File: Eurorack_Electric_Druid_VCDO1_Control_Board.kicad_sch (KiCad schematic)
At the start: 0 parts

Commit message: Multiboard work update
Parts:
- added C20, C21, C22, C23: 0.1uF, DIYSynthMNL:C_Rect_L7.0mm_W2.0mm_P5.00mm_BigPads, symbol Device:C
- added H1, H2: MountingHole_Pad, DIYSynthMNL:MountingHole_M3_Standoff_Pad, symbol Mechanical:MountingHole_Pad
- added J10: Glide_time_CV_in, DIYSynthMNL:AudioJack_3.5mm_long_pads, symbol DIYSynthMNL:PJ3001F
- added J11: Bitcrush_CV_in, DIYSynthMNL:AudioJack_3.5mm_long_pads, symbol DIYSynthMNL:PJ3001F
- added J3: Main_osc_out, DIYSynthMNL:AudioJack_3.5mm_long_pads, symbol DIYSynthMNL:PJ3001F
- added J4: Sub_osc_out, DIYSynthMNL:AudioJack_3.5mm_long_pads, symbol DIYSynthMNL:PJ3001F
- added J5: Glide_on_off_CV_in, DIYSynthMNL:AudioJack_3.5mm_long_pads, symbol DIYSynthMNL:PJ3001F
- added J6: Note_CV_in, DIYSynthMNL:AudioJack_3.5mm_long_pads, symbol DIYSynthMNL:PJ3001F
- added J7: FM_CV_in, DIYSynthMNL:AudioJack_3.5mm_long_pads, symbol DIYSynthMNL:PJ3001F
- added J8: WaveSel_CV_in, DIYSynthMNL:AudioJack_3.5mm_long_pads, symbol DIYSynthMNL:PJ3001F
- added J9: SubSel_CV_in, DIYSynthMNL:AudioJack_3.5mm_long_pads, symbol DIYSynthMNL:PJ3001F
- added R23: 10K, DIYSynthMNL:R_quarter_watt_L6.3mm_D2.5mm_P7.62mm, symbol Device:R
- added R40, R41, R42, R43: 1K, DIYSynthMNL:R_quarter_watt_L6.3mm_D2.5mm_P7.62mm, symbol Device:R
- added RV10: 10K_SubWaveSel, DIYSynthMNL:Potentiometer_RV09_BigPads, symbol Device:R_Potentiometer
- added RV13: 100K_GlideTime_CV_Amount, DIYSynthMNL:Potentiometer_RV09_BigPads, symbol Device:R_Potentiometer
- added RV14: 100K_GlideTime, DIYSynthMNL:Potentiometer_RV09_BigPads, symbol Device:R_Potentiometer
- added RV15: 100K_Bitcrush, DIYSynthMNL:Potentiometer_RV09_BigPads, symbol Device:R_Potentiometer
- added RV16: 100K_Bitcrush_CV_Amount, DIYSynthMNL:Potentiometer_RV09_BigPads, symbol Device:R_Potentiometer
- added RV3: 100K_FM_CV_Amount, DIYSynthMNL:Potentiometer_RV09_BigPads, symbol Device:R_Potentiometer
- added RV5: 100K_WaveSel_CV_Amount, DIYSynthMNL:Potentiometer_RV09_BigPads, symbol Device:R_Potentiometer
- added RV6: 100K_SubSel_CV_Amount, DIYSynthMNL:Potentiometer_RV09_BigPads, symbol Device:R_Potentiometer
- added RV7: 10K_Freq_Course, DIYSynthMNL:Potentiometer_RV09_BigPads, symbol Device:R_Potentiometer
- added RV8: 10K_Freq_Fine, DIYSynthMNL:Potentiometer_RV09_BigPads, symbol Device:R_Potentiometer
- added RV9: 10K_MainWaveSel, DIYSynthMNL:Potentiometer_RV09_BigPads, symbol Device:R_Potentiometer
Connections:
- new net: R42.2, RV9.2
- new net: J10.T, RV13.3
- new net: J7.T, RV3.3
- new net: J11.TN, RV15.2
- new net: J11.T, RV16.3
- new net: R43.2, RV10.2
- new net: J5.TN, R23.2
- new net: J9.T, RV6.3
- new net: J8.T, RV5.3
- new net: J10.TN, RV14.2
- new net: R41.2, RV8.2
- new net: R40.2, RV7.2
- new net Bitcrush_CV: RV16.2
- new net CB_+5V: R23.1, RV10.3, RV14.3, RV15.3, RV7.3, RV8.3, RV9.3
- new net CB_-5V: RV14.1, RV15.1
- new net CB_GND: C20.2, C21.2, C22.2, C23.2, H1.1, H2.1, J10.S, J11.S, J3.S, J4.S, J5.S, J6.S, RV10.1, RV13.1, RV16.1, RV3.1, RV5.1, RV6.1, RV7.1, RV8.1, RV9.1
- new net FM_CV: RV3.2
- new net Freq_Course_Ctrl: C20.1, R40.1
- new net Freq_Fine_Ctrl: C21.1, R41.1
- new net GND: J7.S, J8.S, J9.S
- new net Glide_OnOff_CV: J5.T
- new net Glide_Time_CV: RV13.2
- new net MainOsc_Out: J3.T
- new net MainWaveSel_CV: RV5.2
- new net MainWaveSel_Ctrl: C22.1, R42.1
- new net Note_CV: J6.T
- new net SubOsc_Out: J4.T
- new net SubWaveSel_CV: RV6.2
- new net SubWaveSel_Ctrl: C23.1, R43.1
- no-connect marks 0 -> 6
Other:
- note added: "+/-5V"
- note added: "0V-5V"
- note added: "0V/5V"
- note added: "10vpp in"
- note added: "Bitcrush CV"
- note added: "Controls/Pots"
- note added: "FM CV"
- note added: "Glide CV"
- note added: "Glide on/off CV"
- note added: "Main Wave Select CV"
- note added: "Note CV"
- note added: "Pots inverted on purpose!"
- note added: "Sub Wave Select CV"

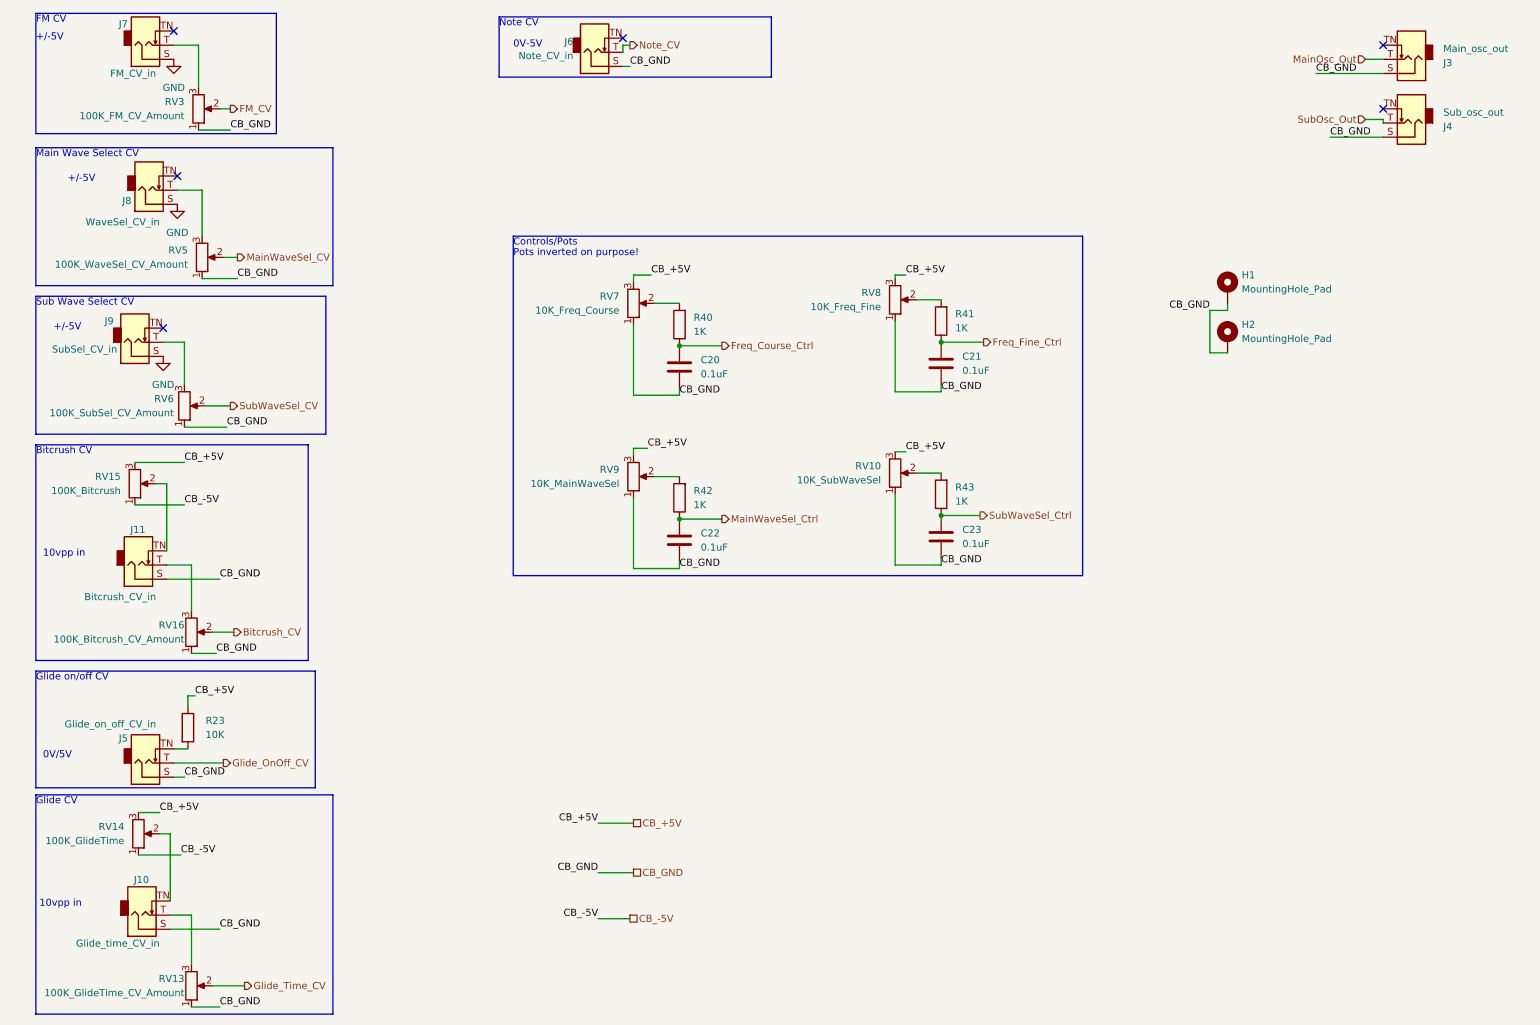
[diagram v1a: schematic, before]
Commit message: updated schematic to rev 0.1.1
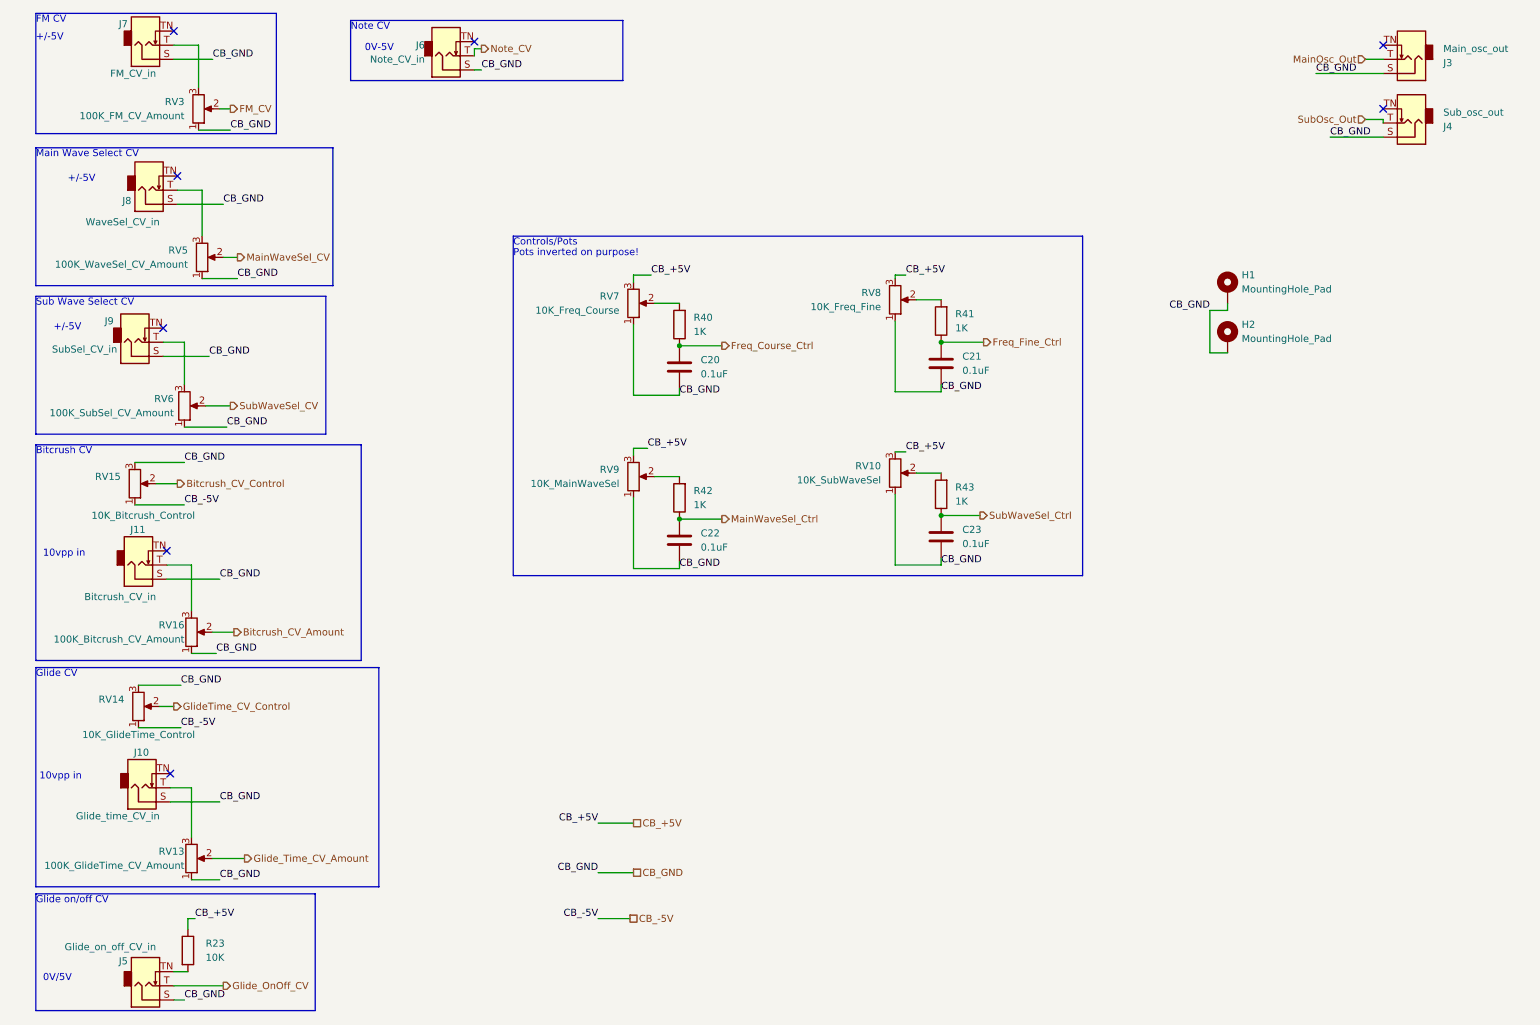
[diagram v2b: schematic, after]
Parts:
- RV14: value 100K_GlideTime -> 10K_GlideTime_Control
- RV15: value 100K_Bitcrush -> 10K_Bitcrush_Control
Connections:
- net GND is gone; now on net CB_GND: J7.S, J8.S, J9.S
- net CB_+5V: no longer RV14.3, RV15.3
- net CB_GND: now also RV14.3, RV15.3
- net at J11.TN: no longer RV15.2
- net at J10.TN: no longer RV14.2
- net Bitcrush_CV renamed Bitcrush_CV_Amount
- net Glide_Time_CV renamed Glide_Time_CV_Amount
- new net Bitcrush_CV_Control: RV15.2
- new net GlideTime_CV_Control: RV14.2
- no-connect marks 6 -> 8
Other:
- moved on the sheet: J10, J5, J6, R23, RV13, RV14

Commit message: updated to schematic revision 1.2
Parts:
- renumbered H1 to H3, H2 to H4
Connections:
- net CB_+5V: now also RV10.1, RV7.1, RV8.1, RV9.1; no longer RV10.3, RV7.3, RV8.3, RV9.3
- net CB_GND: now also RV10.3, RV7.3, RV8.3, RV9.3; no longer RV10.1, RV7.1, RV8.1, RV9.1
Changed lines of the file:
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@@
     (title "Eurorack Electric Druid VCDO1 - Control Board")
     (date "2023-12-30")
-    (rev "0.1.1")
+    (rev "0.1.2")
     (company "DIYSynthMNL")
     (comment 1 "Shared under a CC BY-NC-SA 4.0 license. Some rights reserved.")
@@
   (symbol (lib_id "Mechanical:MountingHole_Pad") (at 227.33 74.295 0) (unit 1)
     (in_bom yes) (on_board yes) (dnp no) (fields_autoplaced)
-    (property "Reference" "H2" (at 229.87 71.755 0)
+    (property "Reference" "H4" (at 229.87 71.755 0)
       (effects (font (size 1.27 1.27)) (justify left))
     )
@@
       (project "Electric Druid VCDO1"
         (path "/1a79e409-2950-446e-9b6e-16f6bf0a888d/c68a14c9-390d-4940-8b6e-7a8e2ca87292"
-          (reference "H2") (unit 1)
+          (reference "H4") (unit 1)
         )
       )
@@
         )
         (path "/1a79e409-2950-446e-9b6e-16f6bf0a888d/c68a14c9-390d-4940-8b6e-7a8e2ca87292"
-          (reference "R42") (unit 1)
+          (reference "R50") (unit 1)
         )
       )
@@
         )
         (path "/1a79e409-2950-446e-9b6e-16f6bf0a888d/c68a14c9-390d-4940-8b6e-7a8e2ca87292"
-          (reference "J7") (unit 1)
+          (reference "J5") (unit 1)
         )
       )
@@
     )
   )
-  (symbol (lib_id "Device:R_Potentiometer") (at 167.64 98.425 0) (mirror x) (unit 1)
-    (in_bom yes) (on_board yes) (dnp no)
-    (property "Reference" "RV10" (at 165.1 97.155 0)
-      (effects (font (size 1.27 1.27)) (justify right))
-    )
-    (property "Value" "10K_SubWaveSel" (at 165.1 99.695 0)
+  (symbol (lib_id "Device:R_Potentiometer") (at 167.64 98.425 0) (unit 1)
+    (in_bom yes) (on_board yes) (dnp no)
+    (property "Reference" "RV10" (at 165.1 99.695 0)
+      (effects (font (size 1.27 1.27)) (justify right))
+    )
+    (property "Value" "10K_SubWaveSel" (at 165.1 97.155 0)
       (effects (font (size 1.27 1.27)) (justify right))
     )
@@
         )
         (path "/1a79e409-2950-446e-9b6e-16f6bf0a888d/c68a14c9-390d-4940-8b6e-7a8e2ca87292"
-          (reference "RV10") (unit 1)
+          (reference "RV9") (unit 1)
         )
       )
@@
         )
         (path "/1a79e409-2950-446e-9b6e-16f6bf0a888d/c68a14c9-390d-4940-8b6e-7a8e2ca87292"
-          (reference "C22") (unit 1)
+          (reference "C24") (unit 1)
         )
       )
@@
         )
         (path "/1a79e409-2950-446e-9b6e-16f6bf0a888d/c68a14c9-390d-4940-8b6e-7a8e2ca87292"
-          (reference "J10") (unit 1)
+          (reference "J11") (unit 1)
         )
       )
@@
         )
         (path "/1a79e409-2950-446e-9b6e-16f6bf0a888d/c68a14c9-390d-4940-8b6e-7a8e2ca87292"
-          (reference "R23") (unit 1)
+          (reference "R51") (unit 1)
         )
       )
@@
         )
         (path "/1a79e409-2950-446e-9b6e-16f6bf0a888d/c68a14c9-390d-4940-8b6e-7a8e2ca87292"
-          (reference "J9") (unit 1)
+          (reference "J10") (unit 1)
         )
       )
@@
         )
         (path "/1a79e409-2950-446e-9b6e-16f6bf0a888d/c68a14c9-390d-4940-8b6e-7a8e2ca87292"
-          (reference "J3") (unit 1)
+          (reference "J7") (unit 1)
         )
       )
@@
         )
         (path "/1a79e409-2950-446e-9b6e-16f6bf0a888d/c68a14c9-390d-4940-8b6e-7a8e2ca87292"
-          (reference "RV6") (unit 1)
+          (reference "RV8") (unit 1)
         )
       )
@@
         )
         (path "/1a79e409-2950-446e-9b6e-16f6bf0a888d/c68a14c9-390d-4940-8b6e-7a8e2ca87292"
-          (reference "J4") (unit 1)
+          (reference "J8") (unit 1)
         )
       )
@@
         )
         (path "/1a79e409-2950-446e-9b6e-16f6bf0a888d/c68a14c9-390d-4940-8b6e-7a8e2ca87292"
-          (reference "J8") (unit 1)
+          (reference "J9") (unit 1)
         )
       )
@@
         )
         (path "/1a79e409-2950-446e-9b6e-16f6bf0a888d/c68a14c9-390d-4940-8b6e-7a8e2ca87292"
-          (reference "C20") (unit 1)
+          (reference "C22") (unit 1)
         )
       )
@@
         )
         (path "/1a79e409-2950-446e-9b6e-16f6bf0a888d/c68a14c9-390d-4940-8b6e-7a8e2ca87292"
-          (reference "J11") (unit 1)
-        )
-      )
-    )
-  )
-  (symbol (lib_id "Device:R_Potentiometer") (at 167.64 67.31 0) (mirror x) (unit 1)
-    (in_bom yes) (on_board yes) (dnp no)
-    (property "Reference" "RV8" (at 165.1 66.04 0)
-      (effects (font (size 1.27 1.27)) (justify right))
-    )
-    (property "Value" "10K_Freq_Fine" (at 165.1 68.58 0)
+          (reference "J12") (unit 1)
+        )
+      )
+    )
+  )
+  (symbol (lib_id "Device:R_Potentiometer") (at 167.64 67.31 0) (unit 1)
+    (in_bom yes) (on_board yes) (dnp no)
+    (property "Reference" "RV8" (at 165.1 68.58 0)
+      (effects (font (size 1.27 1.27)) (justify right))
+    )
+    (property "Value" "10K_Freq_Fine" (at 165.1 66.04 0)
       (effects (font (size 1.27 1.27)) (justify right))
     )
@@
         )
         (path "/1a79e409-2950-446e-9b6e-16f6bf0a888d/c68a14c9-390d-4940-8b6e-7a8e2ca87292"
-          (reference "RV8") (unit 1)
+          (reference "RV6") (unit 1)
         )
       )
@@
   (symbol (lib_id "Mechanical:MountingHole_Pad") (at 227.33 65.405 0) (unit 1)
     (in_bom yes) (on_board yes) (dnp no) (fields_autoplaced)
-    (property "Reference" "H1" (at 229.87 62.865 0)
+    (property "Reference" "H3" (at 229.87 62.865 0)
       (effects (font (size 1.27 1.27)) (justify left))
     )
@@
       (project "Electric Druid VCDO1"
         (path "/1a79e409-2950-446e-9b6e-16f6bf0a888d/c68a14c9-390d-4940-8b6e-7a8e2ca87292"
-          (reference "H1") (unit 1)
-        )
-      )
-    )
-  )
-  (symbol (lib_id "Device:R_Potentiometer") (at 120.65 67.945 0) (mirror x) (unit 1)
-    (in_bom yes) (on_board yes) (dnp no)
-    (property "Reference" "RV7" (at 118.11 66.675 0)
-      (effects (font (size 1.27 1.27)) (justify right))
-    )
-    (property "Value" "10K_Freq_Course" (at 118.11 69.215 0)
+          (reference "H3") (unit 1)
+        )
+      )
+    )
+  )
+  (symbol (lib_id "Device:R_Potentiometer") (at 120.65 67.945 0) (unit 1)
+    (in_bom yes) (on_board yes) (dnp no)
+    (property "Reference" "RV7" (at 118.11 69.215 0)
+      (effects (font (size 1.27 1.27)) (justify right))
+    )
+    (property "Value" "10K_Freq_Course" (at 118.11 66.675 0)
       (effects (font (size 1.27 1.27)) (justify right))
     )
@@
     )
   )
-  (symbol (lib_id "Device:R_Potentiometer") (at 120.65 99.06 0) (mirror x) (unit 1)
-    (in_bom yes) (on_board yes) (dnp no)
-    (property "Reference" "RV9" (at 118.11 97.79 0)
-      (effects (font (size 1.27 1.27)) (justify right))
-    )
-    (property "Value" "10K_MainWaveSel" (at 118.11 100.33 0)
+  (symbol (lib_id "Device:R_Potentiometer") (at 120.65 99.06 0) (unit 1)
+    (in_bom yes) (on_board yes) (dnp no)
+    (property "Reference" "RV9" (at 118.11 100.33 0)
+      (effects (font (size 1.27 1.27)) (justify right))
+    )
+    (property "Value" "10K_MainWaveSel" (at 118.11 97.79 0)
       (effects (font (size 1.27 1.27)) (justify right))
     )
@@
         )
         (path "/1a79e409-2950-446e-9b6e-16f6bf0a888d/c68a14c9-390d-4940-8b6e-7a8e2ca87292"
-          (reference "RV9") (unit 1)
+          (reference "RV10") (unit 1)
         )
       )
@@
         )
         (path "/1a79e409-2950-446e-9b6e-16f6bf0a888d/c68a14c9-390d-4940-8b6e-7a8e2ca87292"
-          (reference "R41") (unit 1)
+          (reference "R47") (unit 1)
         )
       )
@@
         )
         (path "/1a79e409-2950-446e-9b6e-16f6bf0a888d/c68a14c9-390d-4940-8b6e-7a8e2ca87292"
-          (reference "RV3") (unit 1)
+          (reference "RV4") (unit 1)
         )
       )
@@
         )
         (path "/1a79e409-2950-446e-9b6e-16f6bf0a888d/c68a14c9-390d-4940-8b6e-7a8e2ca87292"
-          (reference "R40") (unit 1)
+          (reference "R48") (unit 1)
         )
       )
@@
         )
         (path "/1a79e409-2950-446e-9b6e-16f6bf0a888d/c68a14c9-390d-4940-8b6e-7a8e2ca87292"
-          (reference "J5") (unit 1)
+          (reference "J13") (unit 1)
         )
       )
@@
         )
         (path "/1a79e409-2950-446e-9b6e-16f6bf0a888d/c68a14c9-390d-4940-8b6e-7a8e2ca87292"
-          (reference "R43") (unit 1)
-        )
-      )
+          (reference "R49") (unit 1)
+        )
+      )
